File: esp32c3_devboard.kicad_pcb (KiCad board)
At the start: 2 copper layers, 41.9 x 30 mm, 60 parts, among them J1 Micro_USB, J3 Conn_01x15_Male, J4 Conn_01x15_Male, SW1 RST, SW2 BOOT, U1 ESP32-C3-MINI-1, U2 SRV05-4, U3 AMS1117-3.3, U4 CP2102N-A01-GQFN28, U5 USB2514B_Bi, Y1 24MHz

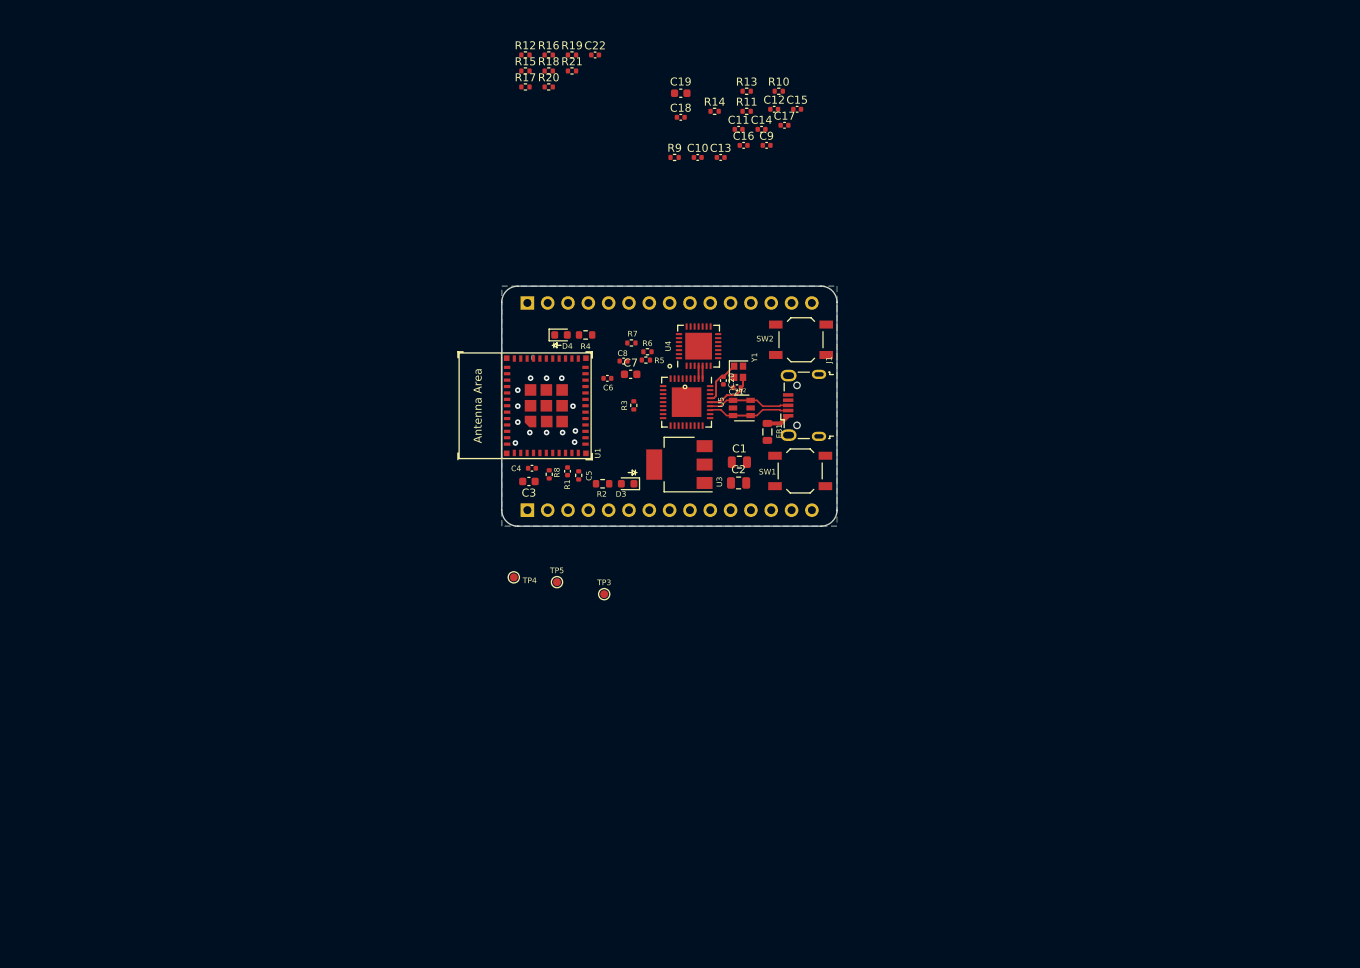
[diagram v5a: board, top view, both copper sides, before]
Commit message: Update schematic to be hierarchical
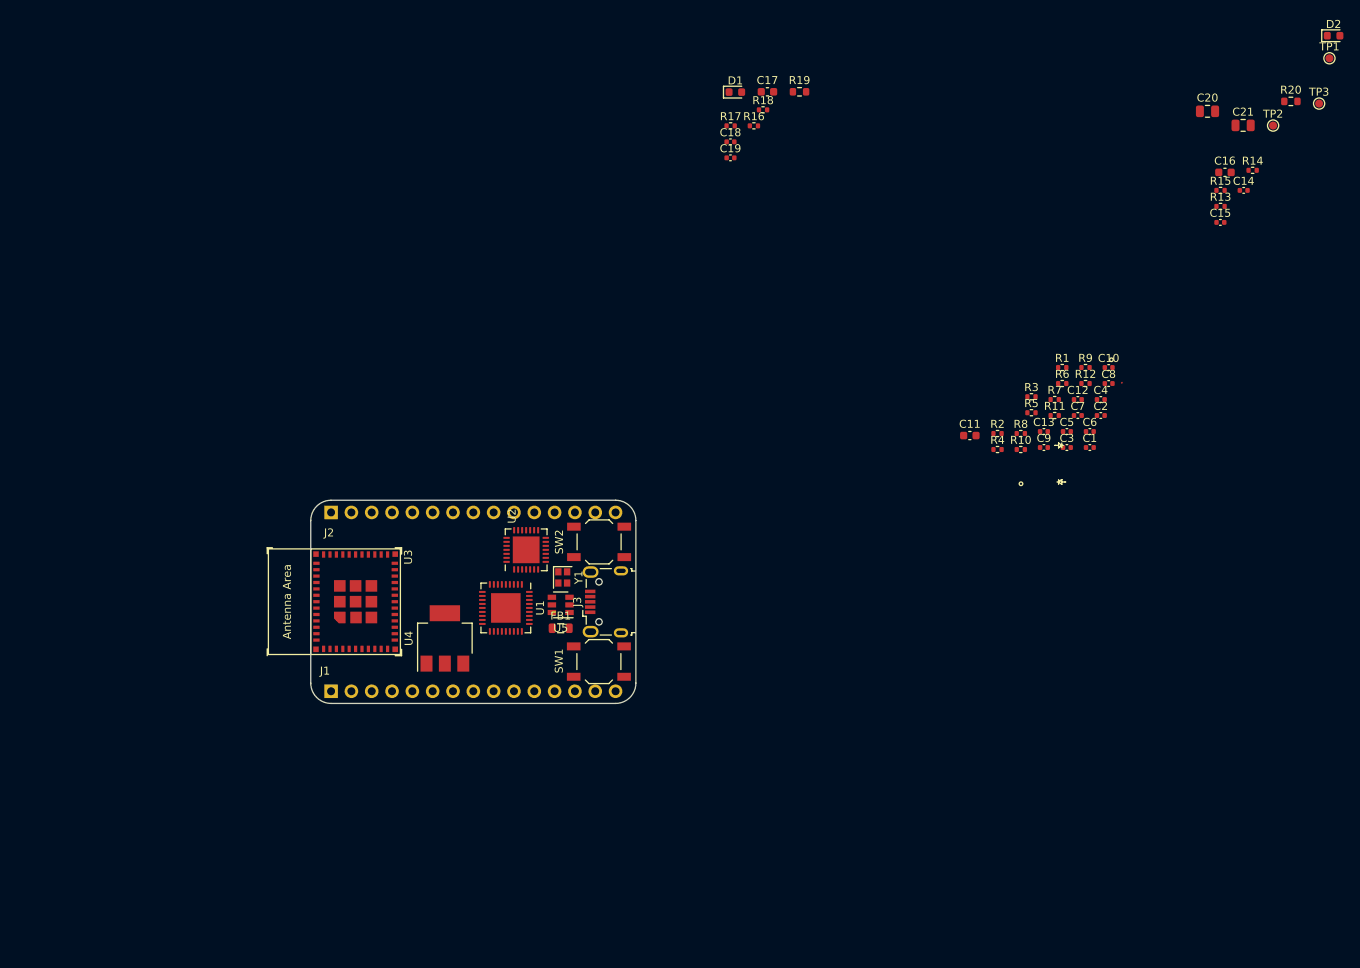
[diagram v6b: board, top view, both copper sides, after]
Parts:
- removed C22: 100n, Capacitor_SMD:C_0402_1005Metric
- removed D3: PWR_LED, LED_SMD:LED_0603_1608Metric
- removed D4: USR_LED, LED_SMD:LED_0603_1608Metric
- removed J4: Conn_01x15_Male, Connector_PinHeader_2.54mm:PinHeader_1x15_P2.54mm_Vertical
- removed R21: 10K, Resistor_SMD:R_0402_1005Metric
- removed TP4: TP_3V3, TestPoint:TestPoint_Pad_D1.0mm
- removed TP5: TP_GND, TestPoint:TestPoint_Pad_D1.0mm
- added D1: USR_LED, LED_SMD:LED_0603_1608Metric, F.Cu at (162.3, 60.7)
- added D2: PWR_LED, LED_SMD:LED_0603_1608Metric, F.Cu at (237.1, 53.7)
- added J2: Conn_01x15_Male, Connector_PinHeader_2.54mm:PinHeader_1x15_P2.54mm_Vertical, B.Cu at (111.8, 113.3)
- added TP1: TP_5V, TestPoint:TestPoint_Pad_D1.0mm, F.Cu at (236.6, 56.5)
- added TP2: TP_3V3, TestPoint:TestPoint_Pad_D1.0mm, F.Cu at (229.5, 64.9)
- C1: value 22u -> 220n; footprint Capacitor_SMD:C_0805_2012Metric -> Capacitor_SMD:C_0402_1005Metric
- C10: value 220n -> 100n
- C11: value 100n -> 1u; footprint Capacitor_SMD:C_0402_1005Metric -> Capacitor_SMD:C_0603_1608Metric
- C12, C13: value 100n -> 18p
- C14: value 100n -> 1uF
- C16, C17: value 100n -> 10u; footprint Capacitor_SMD:C_0402_1005Metric -> Capacitor_SMD:C_0603_1608Metric
- C19: value 1u -> 1uF; footprint Capacitor_SMD:C_0603_1608Metric -> Capacitor_SMD:C_0402_1005Metric
- C2: value 22u -> 100n; footprint Capacitor_SMD:C_0805_2012Metric -> Capacitor_SMD:C_0402_1005Metric
- C20, C21: value 18p -> 10u; footprint Capacitor_SMD:C_0402_1005Metric -> Capacitor_SMD:C_0805_2012Metric
- C3: value 10u -> 1u; footprint Capacitor_SMD:C_0603_1608Metric -> Capacitor_SMD:C_0402_1005Metric
- C5, C8: value 1uF -> 100n
- C7: value 10u -> 100n; footprint Capacitor_SMD:C_0603_1608Metric -> Capacitor_SMD:C_0402_1005Metric
- C9: value 1u -> 100n
- J1: value Micro_USB -> Conn_01x15_Male; footprint Connector_USB:USB_Micro-B_Wuerth_629105150521 -> Connector_PinHeader_2.54mm:PinHeader_1x15_P2.54mm_Vertical; moved to B.Cu
- J3: value Conn_01x15_Male -> Micro_USB; footprint Connector_PinHeader_2.54mm:PinHeader_1x15_P2.54mm_Vertical -> Connector_USB:USB_Micro-B_Wuerth_629105150521; moved to F.Cu
- R1, R12, R3: value 10K -> 100K
- R11, R16, R9: value 100K -> 10K
- R13: value 12K,1% -> 24K
- R14: value 100K -> 47K
- R15: value 10K -> 4K7
- R17: value 330R -> 10K
- R19: value 10K -> 470Ω; footprint Resistor_SMD:R_0402_1005Metric -> Resistor_SMD:R_0603_1608Metric
- R2: value 1K -> 12K,1%; footprint Resistor_SMD:R_0603_1608Metric -> Resistor_SMD:R_0402_1005Metric
- R20: value 10K -> 1K; footprint Resistor_SMD:R_0402_1005Metric -> Resistor_SMD:R_0603_1608Metric
- R4: value 470Ω -> 100K; footprint Resistor_SMD:R_0603_1608Metric -> Resistor_SMD:R_0402_1005Metric
- R5: value 24K -> 10K
- R6: value 47K -> 10K
- R7: value 4K7 -> 10K
- SW1: value RST -> BOOT
- SW2: value BOOT -> RST
- TP3: value TP_5V -> TP_GND
- U1: value ESP32-C3-MINI-1 -> USB2514B_Bi; footprint Espressif:ESP32-C3-MINI-1 -> Package_DFN_QFN:QFN-36-1EP_6x6mm_P0.5mm_EP3.7x3.7mm
- U2: value SRV05-4 -> CP2102N-A01-GQFN28; footprint Package_TO_SOT_SMD:SOT-23-6 -> Package_DFN_QFN:QFN-28-1EP_5x5mm_P0.5mm_EP3.35x3.35mm
- U3: value AMS1117-3.3 -> ESP32-C3-MINI-1; footprint Package_TO_SOT_SMD:SOT-223-3_TabPin2 -> Espressif:ESP32-C3-MINI-1
- U4: value CP2102N-A01-GQFN28 -> AMS1117-3.3; footprint Package_DFN_QFN:QFN-28-1EP_5x5mm_P0.5mm_EP3.35x3.35mm -> Package_TO_SOT_SMD:SOT-223-3_TabPin2
- U5: value USB2514B_Bi -> SRV05-4; footprint Package_DFN_QFN:QFN-36-1EP_6x6mm_P0.5mm_EP3.7x3.7mm -> Package_TO_SOT_SMD:SOT-23-6
- moved TP3 108.4 mm to (235.3, 62.2)
- moved R20 92.8 mm to (231.7, 61.9)
- moved R15 88.2 mm to (222.9, 73.0)
- moved R12 81.2 mm to (206.1, 97.2)
- moved C4 71.6 mm to (208.0, 99.2), turned to 0 degrees
- moved C21 71.3 mm to (225.8, 64.9)
- moved C20 69.2 mm to (221.3, 63.1), turned to 0 degrees
- moved J1 69.0 mm to (111.8, 135.6), turned to 270 degrees
- moved R14 67.7 mm to (227.0, 70.5)
- moved C3 67.4 mm to (203.7, 105.2), turned to 0 degrees
- moved C5 62.6 mm to (203.7, 103.2), turned to 0 degrees
- moved R1 61.9 mm to (203.2, 95.2), turned to 0 degrees
- moved R13 61.0 mm to (222.9, 75.0)
- moved C14 60.7 mm to (225.8, 73.0)
- moved C8 60.7 mm to (209.0, 97.2)
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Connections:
- C1 pad 1: +5V -> Net-(C1-Pad1)
- C10 pad 1: Net-(C10-Pad1) -> +3V3
- C11 pad 1: Net-(C11-Pad1) -> +3V3
- C12 pad 1: Net-(C12-Pad1) -> GND
- C12 pad 2: GND -> /USB hub/XTALIN
- C13 pad 1: +3V3 -> GND
- C13 pad 2: GND -> /USB hub/XTALOUT
- C14 pad 1: +3V3 -> /USB-UART bridge/VBUS
- C19 pad 1: +3V3 -> /ESP32-C3 module/UART_RTS
- C2 pad 1: +3V3 -> Net-(C2-Pad1)
- C20 pad 1: GND -> +5V
- C20 pad 2: USB_XTALIN -> GND
- C21 pad 1: GND -> +3V3
- C21 pad 2: USB_XTALOUT -> GND
- C3 pad 1: +3V3 -> +5V
- C4 pad 1: +3V3 -> Net-(C4-Pad1)
- C5 pad 1: CHIP_PU -> +3V3
- C8 pad 1: /VBUS -> +3V3
- C9 pad 1: +5V -> +3V3
- FB1 pad 2: /5V_UP_USB -> /USB connector and power supply/5V_USB
- J1 pad 1: /5V_UP_USB -> GND
- J1 pad 2: UP_USB_D- -> +3V3
- J1 pad 3: UP_USB_D+ -> +3V3
- J1 pad 4: (no net) -> /ESP32-C3 module/GPIO2
- J1 pad 5: GND -> /ESP32-C3 module/GPIO3
- J1 pad 6: Net-(C22-Pad1) -> GND
- J3 pad 1: GND -> /USB connector and power supply/5V_USB
- J3 pad 2: +3V3 -> /USB hub/UPSTREAM_USB_D-
- J3 pad 3: +3V3 -> /USB hub/UPSTREAM_USB_D+
- J3 pad 4: GPIO2 -> (no net)
- J3 pad 5: GPIO3 -> GND
- J3 pad 6: GND -> Net-(J3-Pad6)
- R1 pad 2: CHIP_PU -> Net-(C1-Pad1)
- R10 pad 2: CFG_SEL0 -> /USB hub/CFG_SEL0
- R11 pad 1: Net-(R11-Pad1) -> +3V3
- R11 pad 2: +5V -> /USB hub/NON_REM1
- R12 pad 1: +3V3 -> GND
- R12 pad 2: CFG_SEL1 -> /USB hub/NON_REM0
- R13 pad 1: Net-(R13-Pad1) -> +5V
- R13 pad 2: GND -> /USB-UART bridge/VBUS
- R14 pad 1: Net-(R11-Pad1) -> /USB-UART bridge/VBUS
- R15 pad 2: NON_REM1 -> /USB-UART bridge/RSTb
- R16 pad 1: GND -> +3V3
- R16 pad 2: NON_REM0 -> /ESP32-C3 module/GPIO2
- R17 pad 1: GND -> +3V3
- R17 pad 2: Net-(C22-Pad1) -> /ESP32-C3 module/GPIO8
- R18 pad 1: Net-(R18-Pad1) -> +3V3
- R18 pad 2: +3V3 -> /ESP32-C3 module/UART_RTS
- R19 pad 1: Net-(R19-Pad1) -> /ESP32-C3 module/GPIO8
- R19 pad 2: +3V3 -> /ESP32-C3 module/USR_LED_A
- R2 pad 1: +3V3 -> Net-(R2-Pad1)
- R2 pad 2: /PWR_LED_A -> GND
- R20 pad 1: Net-(R20-Pad1) -> +3V3
- R20 pad 2: +3V3 -> /USB connector and power supply/PWR_LED_A
- R3 pad 1: +3V3 -> Net-(R3-Pad1)
- R3 pad 2: GPIO8 -> +5V
- R4 pad 1: GPIO8 -> Net-(R3-Pad1)
- R4 pad 2: /USR_LED_A -> GND
- R5 pad 1: +5V -> Net-(R5-Pad1)
- R5 pad 2: /VBUS -> +3V3
- R6 pad 1: /VBUS -> Net-(R6-Pad1)
- R6 pad 2: GND -> +3V3
- R7 pad 1: +3V3 -> Net-(R7-Pad1)
- R7 pad 2: /RSTb -> +3V3
- R8 pad 1: +3V3 -> Net-(R8-Pad1)
- R8 pad 2: GPIO2 -> +3V3
- R9 pad 2: Net-(C10-Pad1) -> /USB hub/CFG_SEL1
- SW1 pad 2: CHIP_PU -> /ESP32-C3 module/UART_DTR
- SW2 pad 2: DTR -> /ESP32-C3 module/UART_RTS
- TP3 pad 1: +5V -> GND
- U1 pad 1: GND -> /USB hub/DOWNSTREAM_USB1_D-
- U1 pad 10: (no net) -> +3V3
- U1 pad 12: GPIO0 -> (no net)
- U1 pad 13: GPIO1 -> (no net)
- U1 pad 14: GND -> Net-(C4-Pad1)
- U1 pad 15: (no net) -> +3V3
- U1 pad 16: GPIO10 -> (no net)
- U1 pad 18: GPIO4 -> (no net)
- U1 pad 19: GPIO5 -> (no net)
- U1 pad 2: GND -> /USB hub/DOWNSTREAM_USB1_D+
- U1 pad 20: GPIO6 -> (no net)
- U1 pad 21: GPIO7 -> (no net)
- U1 pad 22: GPIO8 -> /USB hub/NON_REM1
- U1 pad 23: DTR -> +3V3
- U1 pad 24: (no net) -> /USB hub/CFG_SEL0
- U1 pad 25: (no net) -> /USB hub/CFG_SEL1
- U1 pad 26: JTAG_USB_D- -> Net-(C1-Pad1)
- U1 pad 27: JTAG_USB_D+ -> Net-(R3-Pad1)
- U1 pad 28: (no net) -> /USB hub/NON_REM0
- U1 pad 29: (no net) -> +3V3
- U1 pad 3: +3V3 -> /USB hub/DOWNSTREAM_USB2_D-
- U1 pad 30: RXD -> /USB hub/UPSTREAM_USB_D-
- U1 pad 31: TXD -> /USB hub/UPSTREAM_USB_D+
- U1 pad 32: (no net) -> /USB hub/XTALOUT
- U1 pad 33: (no net) -> /USB hub/XTALIN
- U1 pad 34: (no net) -> Net-(C2-Pad1)
- U1 pad 35: (no net) -> Net-(R2-Pad1)
- U1 pad 36: GND -> +3V3
- U1 pad 4: (no net) -> /USB hub/DOWNSTREAM_USB2_D+
- U1 pad 5: GPIO2 -> +3V3
- U1 pad 6: GPIO3 -> Net-(R5-Pad1)
- U1 pad 7: (no net) -> Net-(R7-Pad1)
- U1 pad 8: CHIP_PU -> Net-(R6-Pad1)
- U1 pad 9: (no net) -> Net-(R8-Pad1)
- U2 pad 1: UP_USB_D- -> (no net)
- U2 pad 2: GND -> (no net)
- U2 pad 3: UP_USB_D+ -> GND
- U2 pad 4: UP_USB_D+ -> /USB hub/DOWNSTREAM_USB1_D+
- U2 pad 5: +5V -> /USB hub/DOWNSTREAM_USB1_D-
- U2 pad 6: UP_USB_D- -> +3V3
- U3 pad 2: +3V3 -> GND
- U3 pad 3: +5V -> +3V3
- U4 pad 1: (no net) -> GND
- U4 pad 2: (no net) -> +3V3
- U4 pad 3: GND -> +5V
- U5 pad 1: UART_USB_D- -> /USB hub/UPSTREAM_USB_D-
- U5 pad 2: UART_USB_D+ -> GND
- U5 pad 3: JTAG_USB_D- -> /USB hub/UPSTREAM_USB_D+
- U5 pad 4: JTAG_USB_D+ -> /USB hub/UPSTREAM_USB_D+
- U5 pad 5: +3V3 -> +5V
- U5 pad 6: Net-(R18-Pad1) -> /USB hub/UPSTREAM_USB_D-
- Y1 pad 1: USB_XTALIN -> /USB hub/XTALIN
- Y1 pad 3: USB_XTALOUT -> /USB hub/XTALOUT
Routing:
- net UP_USB_D-: track 10.8 -> 0.00 mm
- net UP_USB_D+: track 10.8 -> 0.00 mm
- net USB_XTALOUT: track 6.18 -> 0.00 mm
- net USB_XTALIN: track 5.72 -> 0.00 mm
- net /5V_UP_USB: track 2.99 -> 0.00 mm
- net UART_USB_D-: track 1.61 -> 0.00 mm
- net UART_USB_D+: track 1.61 -> 0.00 mm
- net GND: track 0.53 -> 0.07 mm, vias 13 -> 0
- removed copper zone on B.Cu, net GND
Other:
- board size 41.9 x 30 mm -> 40.6 x 25.4 mm

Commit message: Replace CP2102 with CH340X
Also add BJTs to ESP32C3 strapping pins
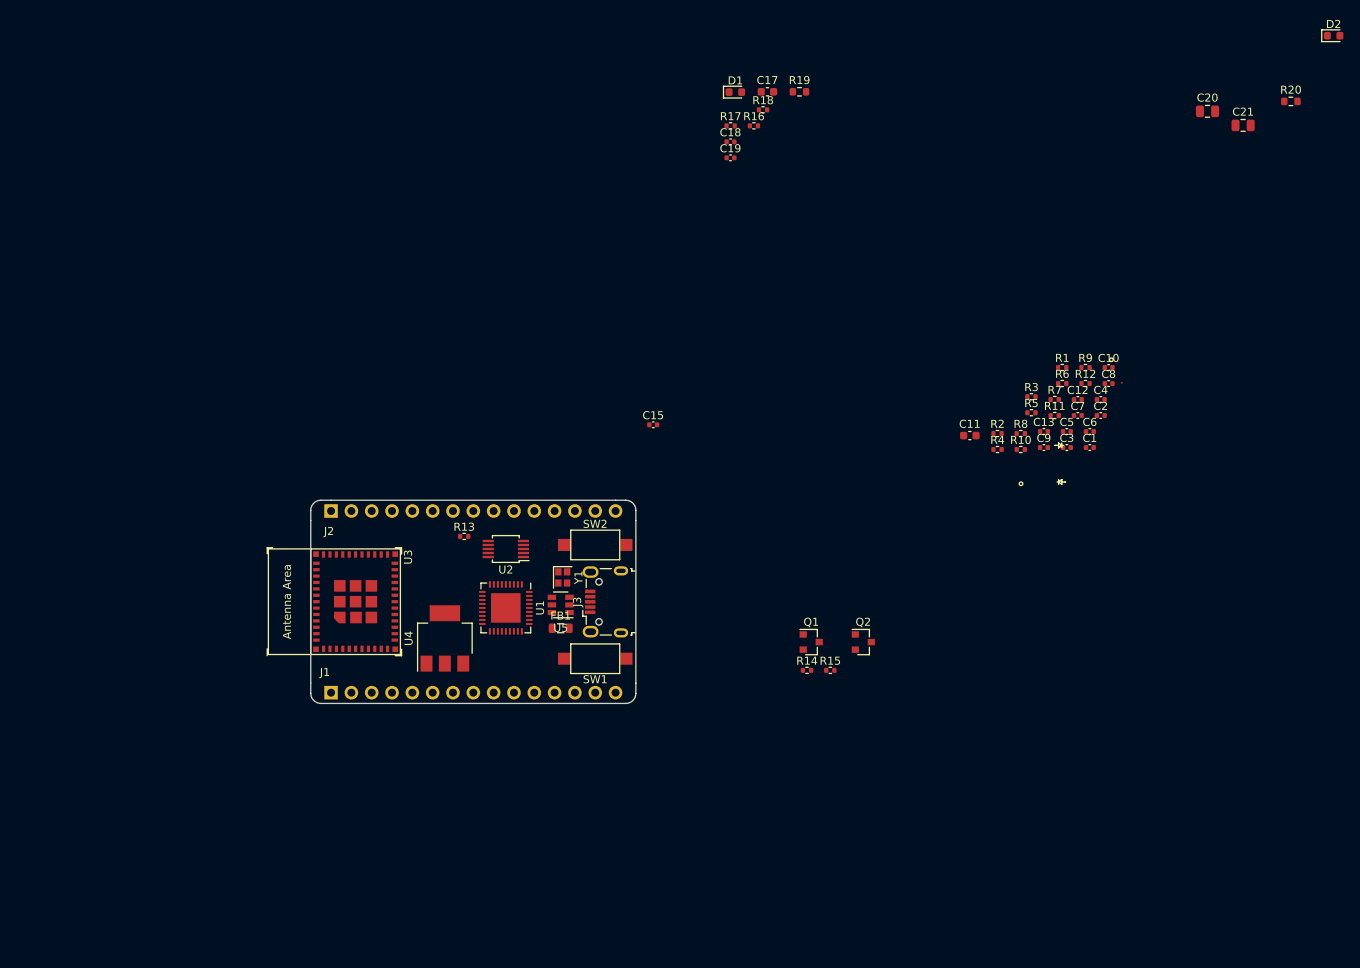
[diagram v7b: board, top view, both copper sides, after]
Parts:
- removed C14: 1uF, Capacitor_SMD:C_0402_1005Metric
- removed C16: 10u, Capacitor_SMD:C_0603_1608Metric
- removed TP1: TP_5V, TestPoint:TestPoint_Pad_D1.0mm
- removed TP2: TP_3V3, TestPoint:TestPoint_Pad_D1.0mm
- removed TP3: TP_GND, TestPoint:TestPoint_Pad_D1.0mm
- added Q1: S8050, Package_TO_SOT_SMD:SOT-23, F.Cu at (171.8, 129.5)
- added Q2: S8050, Package_TO_SOT_SMD:SOT-23, F.Cu at (178.3, 129.5)
- R13: value 24K -> 4K7
- R14: value 47K -> 10K
- R15: value 4K7 -> 10K
- SW1, SW2: footprint Button_Switch_SMD:SW_SPST_TL3342 -> Button_Switch_SMD:SW_SPST_CK_RS282G05A3
- U2: value CP2102N-A01-GQFN28 -> CH340X; footprint Package_DFN_QFN:QFN-28-1EP_5x5mm_P0.5mm_EP3.35x3.35mm -> Package_SO:MSOP-10_3x3mm_P0.5mm
- moved R13 103.2 mm to (128.4, 116.3)
- moved R14 83.7 mm to (171.3, 133.0)
- moved R15 77.3 mm to (174.2, 133.0)
- moved C15 75.3 mm to (152.0, 102.3)
- moved U2 2.54 mm to (133.6, 117.9), turned to 180 degrees
- moved SW2 0.61 mm to (144.8, 117.3)
- moved SW1 0.58 mm to (144.8, 131.6)
- moved J2 0.18 mm to (111.8, 113.1)
- moved J1 0.18 mm to (111.8, 135.8)
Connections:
- C19 pad 1: /ESP32-C3 module/UART_RTS -> /ESP32-C3 module/~RST
- J1 pad 7: /ESP32-C3 module/UART_RTS -> /ESP32-C3 module/~RST
- J2 pad 5: /ESP32-C3 module/UART_DTR -> /ESP32-C3 module/GPIO9
- R13 pad 1: +5V -> GND
- R13 pad 2: /USB-UART bridge/VBUS -> /ESP32-C3 module/UART_DTR
- R14 pad 1: /USB-UART bridge/VBUS -> Net-(Q1-Pad2)
- R14 pad 2: GND -> /ESP32-C3 module/UART_DTR
- R15 pad 1: +3V3 -> Net-(Q2-Pad2)
- R15 pad 2: /USB-UART bridge/RSTb -> /ESP32-C3 module/UART_RTS
- R18 pad 2: /ESP32-C3 module/UART_RTS -> /ESP32-C3 module/~RST
- SW1 pad 2: /ESP32-C3 module/UART_DTR -> /ESP32-C3 module/GPIO9
- SW2 pad 2: /ESP32-C3 module/UART_RTS -> /ESP32-C3 module/~RST
- U2 pad 1: (no net) -> /USB hub/DOWNSTREAM_USB1_D+
- U2 pad 10: (no net) -> +3V3
- U2 pad 2: (no net) -> /USB hub/DOWNSTREAM_USB1_D-
- U2 pad 4: /USB hub/DOWNSTREAM_USB1_D+ -> /ESP32-C3 module/UART_RTS
- U2 pad 5: /USB hub/DOWNSTREAM_USB1_D- -> (no net)
- U2 pad 6: +3V3 -> /ESP32-C3 module/UART_DTR
- U2 pad 8: /USB-UART bridge/VBUS -> /ESP32-C3 module/UART_RXD
- U2 pad 9: /USB-UART bridge/RSTb -> /USB-UART bridge/UART_RXD
- U3 pad 23: /ESP32-C3 module/UART_DTR -> /ESP32-C3 module/GPIO9
- U3 pad 8: /ESP32-C3 module/UART_RTS -> /ESP32-C3 module/~RST
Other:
- outline, holes or cut-outs redrawn
